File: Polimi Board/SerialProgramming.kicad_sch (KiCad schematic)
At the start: 30 parts, among them J2 USB_B_Micro, J3 Conn_ARM_JTAG_SWD_20, J4 USB_B_Micro, J8 Conn_01x03_Pin, U5 FT2232HL, Y2 12MHz

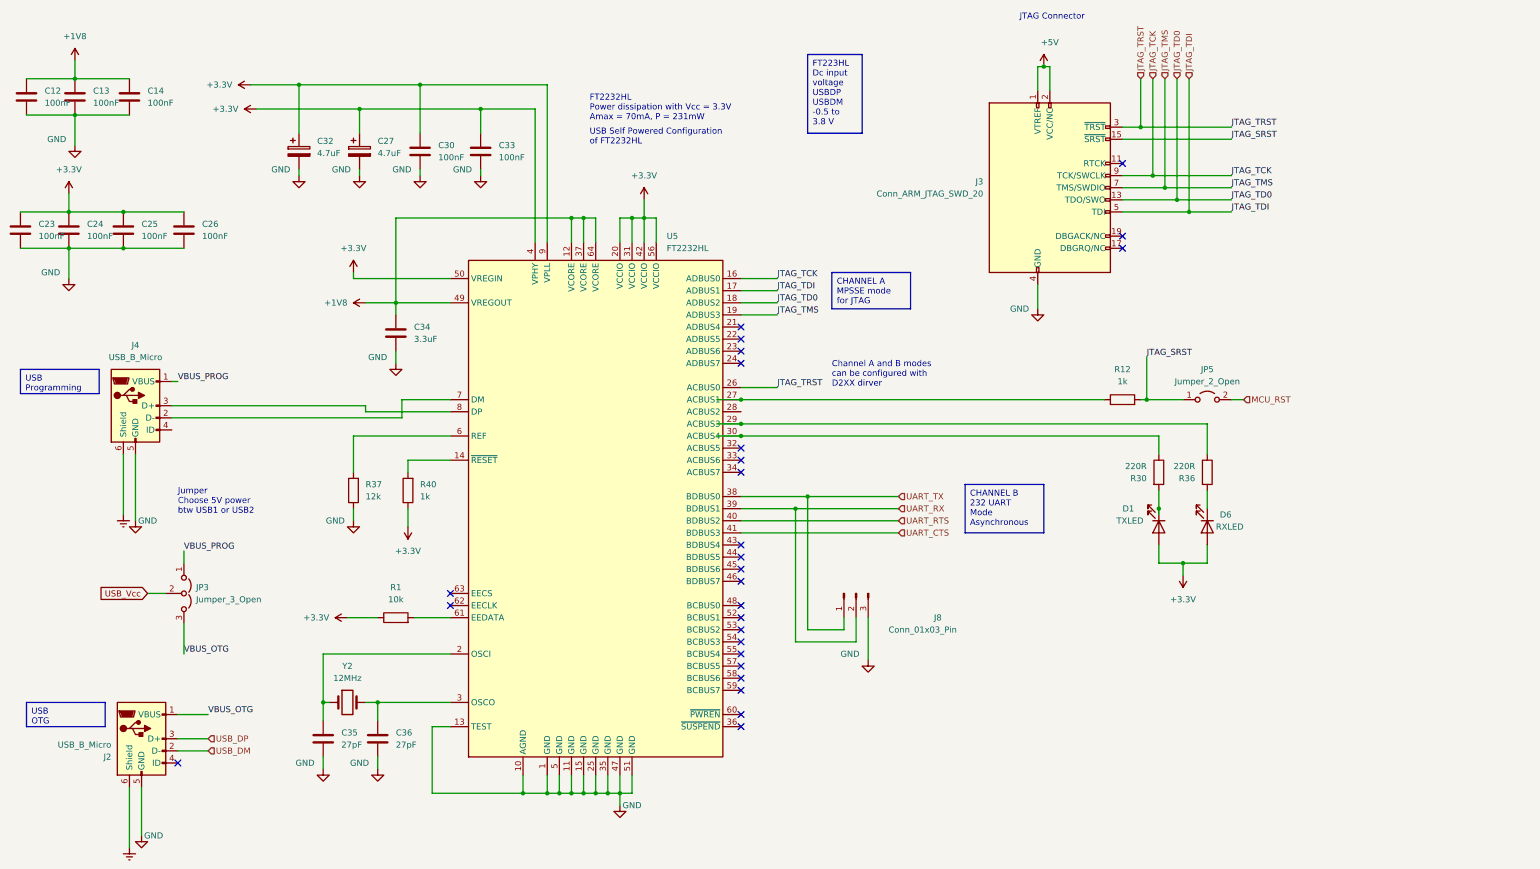
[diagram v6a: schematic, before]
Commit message: adjusted some violations of ERC test
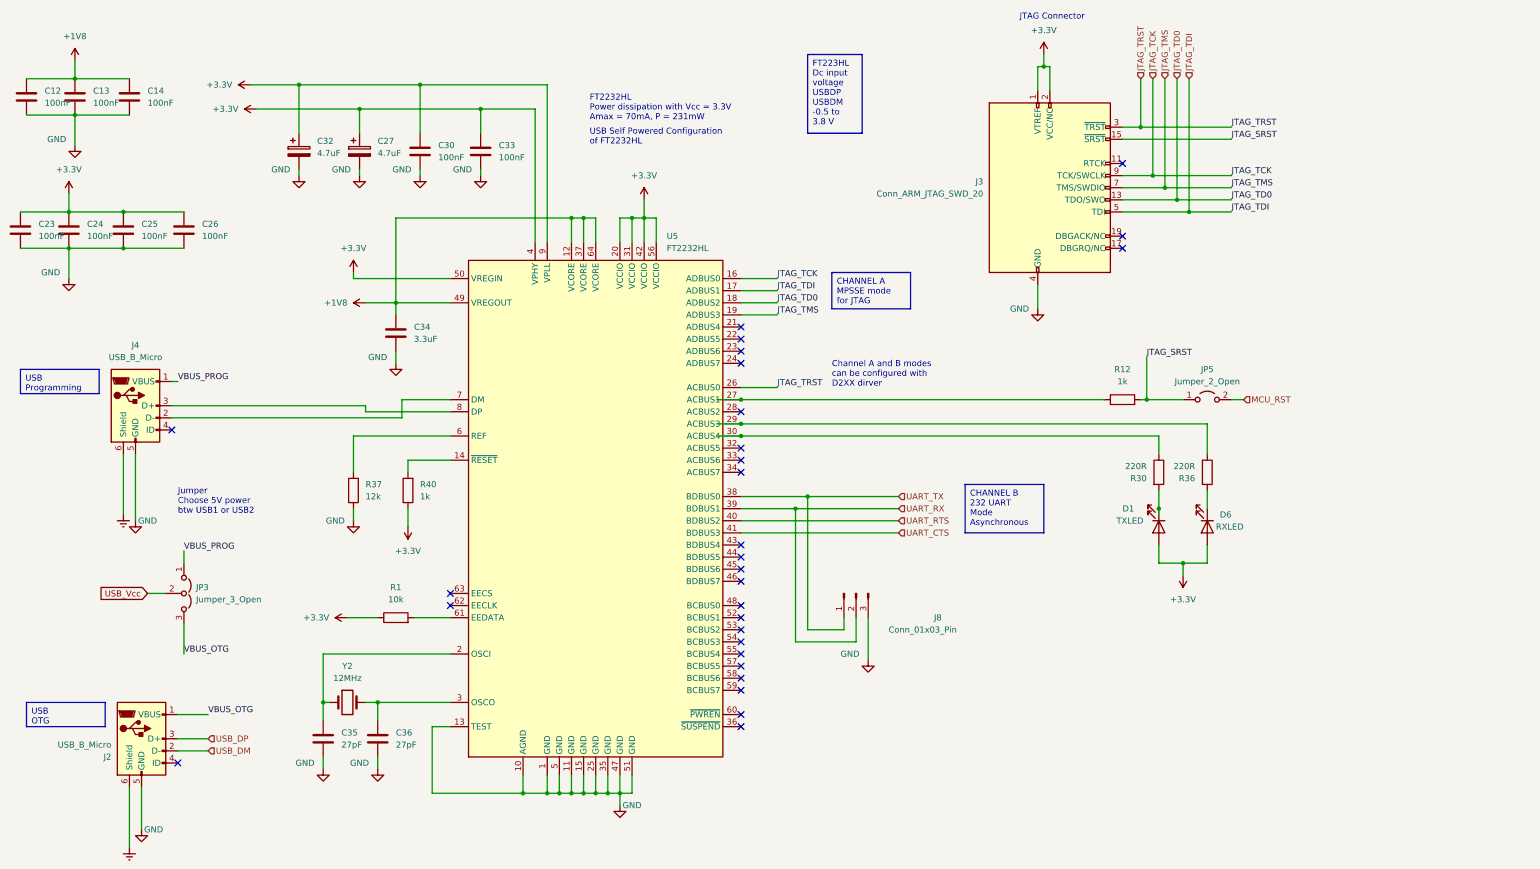
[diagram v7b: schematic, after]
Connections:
- net +5V is gone; now on net +3.3V: J3.1 (VTREF), J3.2 (VCC/NC)
- no-connect marks 27 -> 29
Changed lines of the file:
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@@
   (junction (at 74.93 29.21) (diameter 0) (color 0 0 0 0)
   )
+  (junction (at 231.14 25.4) (diameter 0) (color 0 0 0 0)
+  )
   (junction (at 127 177.8) (diameter 0) (color 0 0 0 0)
   )
@@
   )
   (junction (at 254 48.26) (diameter 0) (color 0 0 0 0)
-  )
-  (junction (at 231.14 25.4) (diameter 0) (color 0 0 0 0)
   )
   (junction (at 91.44 158.75) (diameter 0) (color 0 0 0 0)
@@
   (no_connect (at 49.53 171.45))
   (no_connect (at 167.64 146.05))
+  (no_connect (at 48.26 101.6))
   (no_connect (at 167.64 163.83))
   (no_connect (at 167.64 130.81))
@@
   (no_connect (at 167.64 133.35))
   (no_connect (at 106.68 138.43))
+  (no_connect (at 167.64 97.79))
   (no_connect (at 106.68 135.89))
   (no_connect (at 167.64 128.27))
@@
     (stroke (width 0) (type default))
   )
+  (wire (pts (xy 231.14 22.86) (xy 231.14 25.4))
+    (stroke (width 0) (type default))
+  )
   (wire (pts (xy 167.64 123.19) (xy 200.66 123.19))
     (stroke (width 0) (type default))
@@
     (stroke (width 0) (type default))
   )
+  (wire (pts (xy 231.14 25.4) (xy 232.41 25.4))
+    (stroke (width 0) (type default))
+  )
   (wire (pts (xy 162.56 102.87) (xy 167.64 102.87))
     (stroke (width 0) (type default))
@@
     (stroke (width 0) (type default))
   )
-  (wire (pts (xy 41.91 176.53) (xy 41.91 186.69))
-    (stroke (width 0) (type default))
-  )
   (wire (pts (xy 100.33 29.21) (xy 100.33 39.37))
     (stroke (width 0) (type default))
@@
     (stroke (width 0) (type default))
   )
+  (wire (pts (xy 40.64 106.68) (xy 40.64 120.65))
+    (stroke (width 0) (type default))
+  )
   (wire (pts (xy 256.54 27.94) (xy 256.54 50.8))
     (stroke (width 0) (type default))
@@
     (stroke (width 0) (type default))
   )
+  (wire (pts (xy 251.46 38.1) (xy 270.51 38.1))
+    (stroke (width 0) (type default))
+  )
+  (wire (pts (xy 261.62 55.88) (xy 270.51 55.88))
+    (stroke (width 0) (type default))
+  )
+  (wire (pts (xy 96.52 95.25) (xy 106.68 95.25))
+    (stroke (width 0) (type default))
+  )
+  (wire (pts (xy 247.65 55.88) (xy 261.62 55.88))
+    (stroke (width 0) (type default))
+  )
+  (wire (pts (xy 132.08 57.15) (xy 95.25 57.15))
+    (stroke (width 0) (type default))
+  )
+  (wire (pts (xy 99.06 140.97) (xy 106.68 140.97))
+    (stroke (width 0) (type default))
+  )
+  (wire (pts (xy 80.01 158.75) (xy 81.28 158.75))
+    (stroke (width 0) (type default))
+  )
+  (wire (pts (xy 80.01 158.75) (xy 80.01 162.56))
+    (stroke (width 0) (type default))
+  )
+  (wire (pts (xy 247.65 38.1) (xy 251.46 38.1))
+    (stroke (width 0) (type default))
+  )
+  (wire (pts (xy 137.16 177.8) (xy 139.7 177.8))
+    (stroke (width 0) (type default))
+  )
+  (wire (pts (xy 255.27 118.11) (xy 255.27 114.3))
+    (stroke (width 0) (type default))
+  )
+  (wire (pts (xy 255.27 102.87) (xy 167.64 102.87))
+    (stroke (width 0) (type default))
+  )
+  (wire (pts (xy 254 27.94) (xy 254 48.26))
+    (stroke (width 0) (type default))
+  )
+  (wire (pts (xy 191.77 146.05) (xy 179.07 146.05))
+    (stroke (width 0) (type default))
+  )
+  (wire (pts (xy 251.46 95.25) (xy 252.73 95.25))
+    (stroke (width 0) (type default))
+  )
+  (wire (pts (xy 167.64 115.57) (xy 181.61 115.57))
+    (stroke (width 0) (type default))
+  )
+  (wire (pts (xy 26.67 55.88) (xy 38.1 55.88))
+    (stroke (width 0) (type default))
+  )
+  (wire (pts (xy 181.61 143.51) (xy 181.61 115.57))
+    (stroke (width 0) (type default))
+  )
+  (wire (pts (xy 27.94 35.56) (xy 27.94 41.91))
+    (stroke (width 0) (type default))
+  )
   (wire (pts (xy 38.1 106.68) (xy 38.1 119.38))
     (stroke (width 0) (type default))
   )
-  (wire (pts (xy 251.46 38.1) (xy 270.51 38.1))
-    (stroke (width 0) (type default))
-  )
-  (wire (pts (xy 261.62 55.88) (xy 270.51 55.88))
-    (stroke (width 0) (type default))
-  )
-  (wire (pts (xy 96.52 95.25) (xy 106.68 95.25))
-    (stroke (width 0) (type default))
-  )
-  (wire (pts (xy 247.65 55.88) (xy 261.62 55.88))
-    (stroke (width 0) (type default))
-  )
-  (wire (pts (xy 132.08 57.15) (xy 95.25 57.15))
-    (stroke (width 0) (type default))
-  )
-  (wire (pts (xy 99.06 140.97) (xy 106.68 140.97))
-    (stroke (width 0) (type default))
-  )
-  (wire (pts (xy 80.01 158.75) (xy 81.28 158.75))
-    (stroke (width 0) (type default))
-  )
-  (wire (pts (xy 80.01 158.75) (xy 80.01 162.56))
-    (stroke (width 0) (type default))
-  )
-  (wire (pts (xy 247.65 38.1) (xy 251.46 38.1))
-    (stroke (width 0) (type default))
-  )
-  (wire (pts (xy 137.16 177.8) (xy 139.7 177.8))
-    (stroke (width 0) (type default))
-  )
-  (wire (pts (xy 232.41 25.4) (xy 231.14 25.4))
-    (stroke (width 0) (type default))
-  )
-  (wire (pts (xy 255.27 118.11) (xy 255.27 114.3))
-    (stroke (width 0) (type default))
-  )
-  (wire (pts (xy 255.27 102.87) (xy 167.64 102.87))
-    (stroke (width 0) (type default))
-  )
-  (wire (pts (xy 254 27.94) (xy 254 48.26))
-    (stroke (width 0) (type default))
-  )
-  (wire (pts (xy 191.77 146.05) (xy 179.07 146.05))
-    (stroke (width 0) (type default))
-  )
-  (wire (pts (xy 251.46 95.25) (xy 252.73 95.25))
-    (stroke (width 0) (type default))
-  )
-  (wire (pts (xy 167.64 115.57) (xy 181.61 115.57))
-    (stroke (width 0) (type default))
-  )
-  (wire (pts (xy 26.67 55.88) (xy 38.1 55.88))
-    (stroke (width 0) (type default))
-  )
-  (wire (pts (xy 181.61 143.51) (xy 181.61 115.57))
-    (stroke (width 0) (type default))
-  )
-  (wire (pts (xy 27.94 35.56) (xy 27.94 41.91))
-    (stroke (width 0) (type default))
-  )
   (wire (pts (xy 50.8 142.24) (xy 50.8 148.59))
     (stroke (width 0) (type default))
@@
     (stroke (width 0) (type default))
   )
+  (wire (pts (xy 41.91 176.53) (xy 41.91 185.42))
+    (stroke (width 0) (type default))
+  )
   (wire (pts (xy 17.78 27.94) (xy 27.94 27.94))
     (stroke (width 0) (type default))
@@
   )
   (wire (pts (xy 102.87 177.8) (xy 121.92 177.8))
-    (stroke (width 0) (type default))
-  )
-  (wire (pts (xy 40.64 106.68) (xy 40.64 120.65))
     (stroke (width 0) (type default))
   )
@@
         (path "/319fe76e-1f98-44b3-99b0-af1a9ad7322c/e865888c-a3d0-46cb-8bab-3f3f2de35235"
           (reference "R30") (unit 1)
+        )
+      )
+    )
+  )
+  (symbol (lib_id "power:GND") (at 41.91 185.42 0) (unit 1)
+    (in_bom yes) (on_board yes) (dnp no)
+    (property "Reference" "#PWR01" (at 41.91 191.77 0)
+      (effects (font (size 1.27 1.27)) hide)
+    )
+    (property "Value" "GND" (at 44.45 185.42 0)
+      (effects (font (size 1.27 1.27)))
+    )
+    (property "Footprint" "" (at 41.91 185.42 0)
+      (effects (font (size 1.27 1.27)) hide)
+    )
+    (property "Datasheet" "" (at 41.91 185.42 0)
+      (effects (font (size 1.27 1.27)) hide)
+    )
+    (pin "1")
+    (instances
+      (project "Polimi Board"
+        (path "/319fe76e-1f98-44b3-99b0-af1a9ad7322c/e865888c-a3d0-46cb-8bab-3f3f2de35235"
+          (reference "#PWR01") (unit 1)
         )
       )
@@
     )
   )
-  (symbol (lib_id "power:GND") (at 41.91 186.69 0) (unit 1)
-    (in_bom yes) (on_board yes) (dnp no)
-    (property "Reference" "#PWR01" (at 41.91 193.04 0)
-      (effects (font (size 1.27 1.27)) hide)
-    )
-    (property "Value" "GND" (at 44.45 186.69 0)
-      (effects (font (size 1.27 1.27)))
-    )
-    (property "Footprint" "" (at 41.91 186.69 0)
-      (effects (font (size 1.27 1.27)) hide)
-    )
-    (property "Datasheet" "" (at 41.91 186.69 0)
-      (effects (font (size 1.27 1.27)) hide)
-    )
-    (pin "1")
-    (instances
-      (project "Polimi Board"
-        (path "/319fe76e-1f98-44b3-99b0-af1a9ad7322c/e865888c-a3d0-46cb-8bab-3f3f2de35235"
-          (reference "#PWR01") (unit 1)
-        )
-      )
-    )
-  )
-  (symbol (lib_id "power:+5V") (at 231.14 25.4 0) (unit 1)
-    (in_bom yes) (on_board yes) (dnp no)
-    (property "Reference" "#PWR064" (at 231.14 29.21 0)
-      (effects (font (size 1.27 1.27)) hide)
-    )
-    (property "Value" "+5V" (at 232.41 20.32 0)
-      (effects (font (size 1.27 1.27)))
-    )
-    (property "Footprint" "" (at 231.14 25.4 0)
-      (effects (font (size 1.27 1.27)) hide)
-    )
-    (property "Datasheet" "" (at 231.14 25.4 0)
-      (effects (font (size 1.27 1.27)) hide)
-    )
-    (pin "1")
-    (instances
-      (project "Polimi Board"
-        (path "/319fe76e-1f98-44b3-99b0-af1a9ad7322c/e865888c-a3d0-46cb-8bab-3f3f2de35235"
-          (reference "#PWR064") (unit 1)
-        )
-      )
+  (symbol (lib_id "power:+3.3V") (at 231.14 22.86 0) (unit 1)
+    (in_bom yes) (on_board yes) (dnp no) (fields_autoplaced)
+    (property "Reference" "#PWR020" (at 231.14 26.67 0)
+      (effects (font (size 1.27 1.27)) hide)
+    )
+    (property "Value" "+3.3V" (at 231.14 17.78 0)
+      (effects (font (size 1.27 1.27)))
+    )
+    (property "Footprint" "" (at 231.14 22.86 0)
+      (effects (font (size 1.27 1.27)) hide)
+    )
+    (property "Datasheet" "" (at 231.14 22.86 0)
+      (effects (font (size 1.27 1.27)) hide)
+    )
+    (pin "1")
+    (instances
+      (project "Polimi Board"
+        (path "/319fe76e-1f98-44b3-99b0-af1a9ad7322c/e865888c-a3d0-46cb-8bab-3f3f2de35235"
+          (reference "#PWR020") (unit 1)
+        )
+      )

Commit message: Added footprint from Mouser
readu for wiring
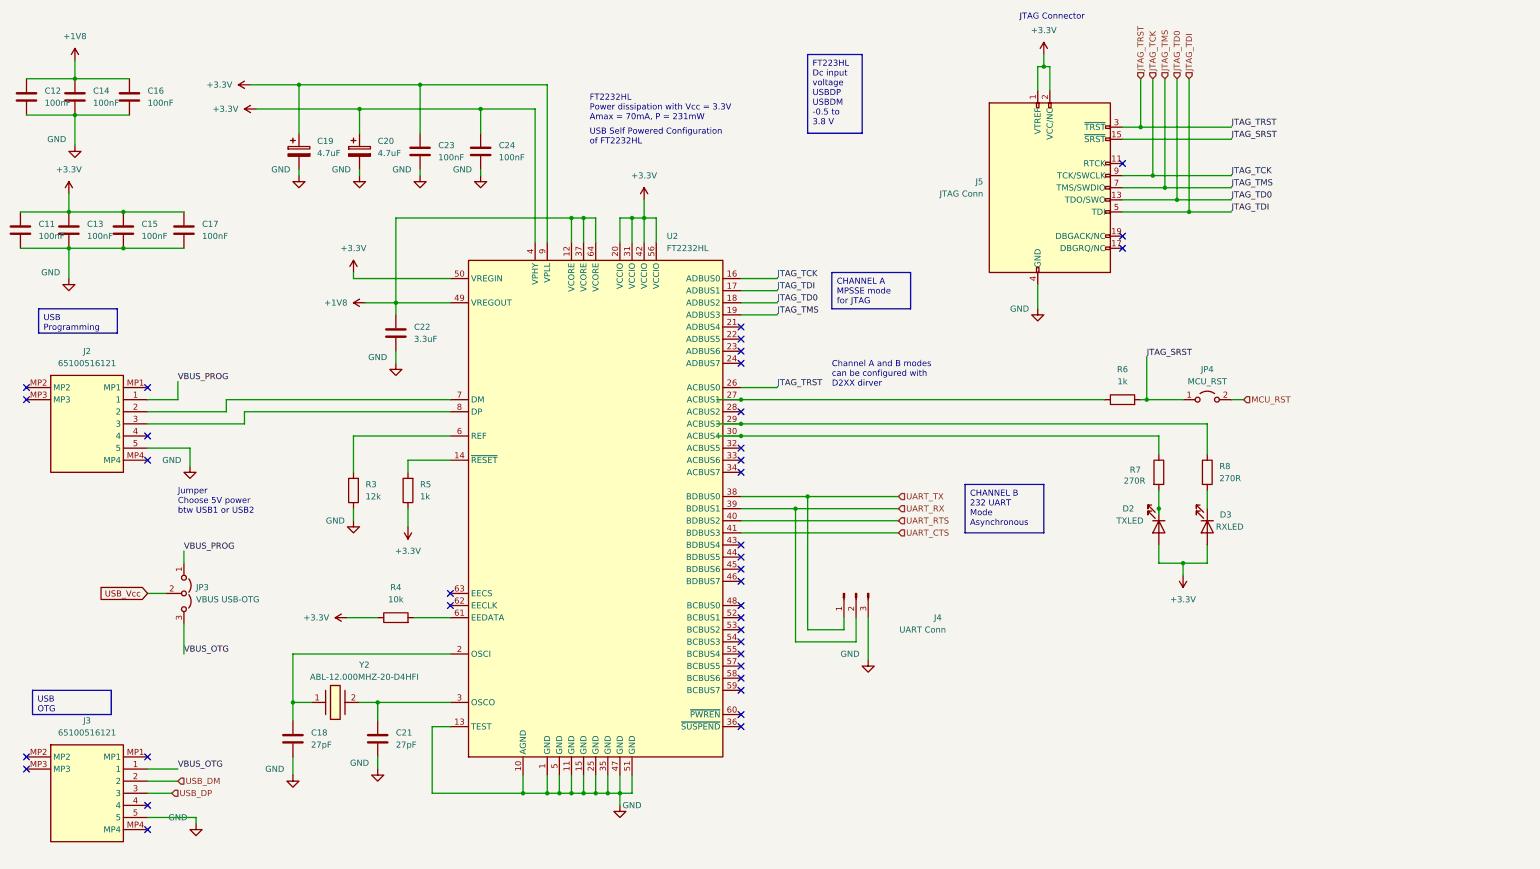
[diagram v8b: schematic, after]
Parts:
- removed J2, J4: USB_B_Micro, symbol Connector:USB_B_Micro
- removed Y2: 12MHz, symbol Device:Crystal
- added J2, J3: 65100516121, SamacSys_Parts:65100516121, symbol SamacSys_Parts:65100516121
- added Y2: ABL-12.000MHZ-20-D4HFI, SamacSys_Parts:ABL, symbol SamacSys_Parts:ABL-12.000MHZ-20-D4HFI
- C11: renamed from C23; footprint (none) -> Capacitor_SMD:C_0603_1608Metric_Pad1.08x0.95mm_HandSolder
- C12: footprint (none) -> Capacitor_SMD:C_0603_1608Metric_Pad1.08x0.95mm_HandSolder
- C13: renamed from C24; footprint (none) -> Capacitor_SMD:C_0603_1608Metric_Pad1.08x0.95mm_HandSolder
- C14: renamed from C13; footprint (none) -> Capacitor_SMD:C_0603_1608Metric_Pad1.08x0.95mm_HandSolder
- C15: renamed from C25; footprint (none) -> Capacitor_SMD:C_0603_1608Metric_Pad1.08x0.95mm_HandSolder
- C16: renamed from C14; footprint (none) -> Capacitor_SMD:C_0603_1608Metric_Pad1.08x0.95mm_HandSolder
- C17: renamed from C26; footprint (none) -> Capacitor_SMD:C_0603_1608Metric_Pad1.08x0.95mm_HandSolder
- C18: renamed from C35; footprint (none) -> Capacitor_SMD:C_0603_1608Metric_Pad1.08x0.95mm_HandSolder
- C19: renamed from C32; footprint Capacitor_SMD:C_0201_0603Metric_Pad0.64x0.40mm_HandSolder -> Capacitor_THT:CP_Radial_D4.0mm_P1.50mm
- C20: renamed from C27; footprint Capacitor_SMD:C_0201_0603Metric_Pad0.64x0.40mm_HandSolder -> Capacitor_THT:CP_Radial_D4.0mm_P1.50mm
- C21: renamed from C36; footprint (none) -> Capacitor_SMD:C_0603_1608Metric_Pad1.08x0.95mm_HandSolder
- C22: renamed from C34; footprint (none) -> Capacitor_SMD:C_0603_1608Metric_Pad1.08x0.95mm_HandSolder
- C23: renamed from C30; footprint (none) -> Capacitor_SMD:C_0603_1608Metric_Pad1.08x0.95mm_HandSolder
- C24: renamed from C33; footprint (none) -> Capacitor_SMD:C_0603_1608Metric_Pad1.08x0.95mm_HandSolder
- D2: renamed from D1; footprint (none) -> LED_THT:LED_D3.0mm
- D3: renamed from D6; footprint (none) -> LED_THT:LED_D3.0mm
- J4: renamed from J8; value Conn_01x03_Pin -> UART Conn
- J5: renamed from J3; value Conn_ARM_JTAG_SWD_20 -> JTAG Conn
- JP3: value Jumper_3_Open -> VBUS USB-OTG; footprint (none) -> Connector_PinHeader_2.54mm:PinHeader_1x03_P2.54mm_Vertical
- JP4: renamed from JP5; value Jumper_2_Open -> MCU_RST; footprint TestPoint:TestPoint_2Pads_Pitch5.08mm_Drill1.3mm -> Connector_PinHeader_2.54mm:PinHeader_1x02_P2.54mm_Vertical
- R3: renamed from R37; footprint (none) -> Resistor_SMD:R_0603_1608Metric_Pad0.98x0.95mm_HandSolder
- R4: renamed from R1; footprint (none) -> Resistor_SMD:R_0603_1608Metric_Pad0.98x0.95mm_HandSolder
- R5: renamed from R40; footprint (none) -> Resistor_SMD:R_0603_1608Metric_Pad0.98x0.95mm_HandSolder
- R6: renamed from R12; footprint (none) -> Resistor_SMD:R_0603_1608Metric_Pad0.98x0.95mm_HandSolder
- R7: renamed from R30; value 220R -> 270R; footprint (none) -> Resistor_SMD:R_0603_1608Metric_Pad0.98x0.95mm_HandSolder
- R8: renamed from R36; value 220R -> 270R; footprint (none) -> Resistor_SMD:R_0603_1608Metric_Pad0.98x0.95mm_HandSolder
- renumbered U5 to U2
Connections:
- net GND: now also J2.5, J3.5
- net USB_DM: now also J3.2
- net USB_DP: now also J3.3
- net VBUS_OTG: now also J3.1
- net VBUS_PROG: now also J2.1
- net at C18.2, U2.2 (OSCI): now also Y2.1
- net at C21.2, U2.3 (OSCO): now also Y2.2
- net at U2.7 (DM): now also J2.2
- net at U2.8 (DP): now also J2.3
- no-connect marks 29 -> 37
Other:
- moved on the sheet: C18
